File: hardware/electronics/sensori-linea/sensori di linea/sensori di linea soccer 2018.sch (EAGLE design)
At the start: 21 parts, among them T1 BP103, T2 BP103, T3 BP103, T4 BP103

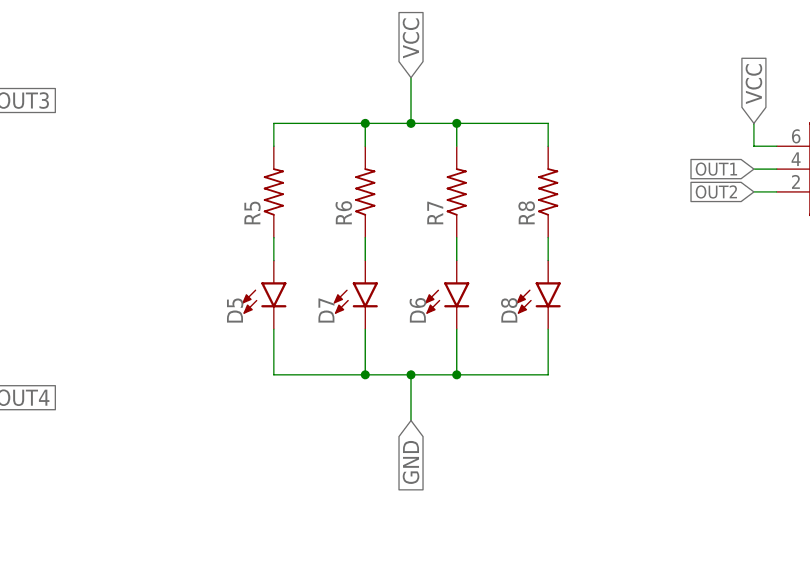
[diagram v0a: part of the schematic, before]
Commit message: modifiche a sensori di linea 2018
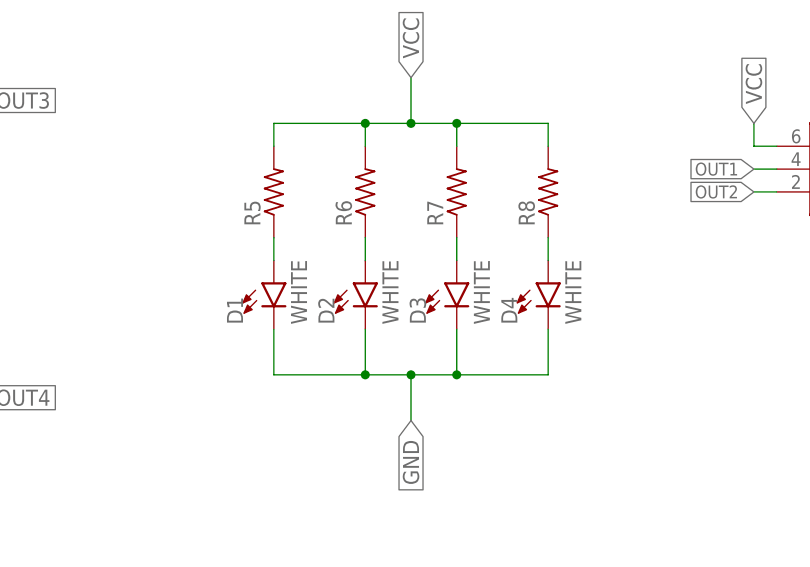
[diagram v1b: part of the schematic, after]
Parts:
- removed D5, D6, D7, D8: (no value), SparkFun-LED:LED1206
- added D1, D2, D3, D4: WHITE, SparkFun-LED:LED-WHITE1206
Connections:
- net GND: now also D1.C, D2.C, D3.C, D4.C; no longer D5.C, D6.C, D7.C, D8.C
- net N$2: now also D1.A; no longer D5.A
- net N$3: now also D2.A; no longer D7.A
- net N$4: now also D3.A; no longer D6.A
- net N$5: now also D4.A; no longer D8.A
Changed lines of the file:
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@@
 <part name="R8" library="rcl" library_urn="urn:adsk.eagle:library:334" deviceset="R-US_" device="0204/7" package3d_urn="urn:adsk.eagle:package:23498/1"/>
 <part name="SV1" library="con-lstb" library_urn="urn:adsk.eagle:library:162" deviceset="MA03-2" device="" package3d_urn="urn:adsk.eagle:package:8334/1"/>
-<part name="D5" library="SparkFun-LED" deviceset="LED" device="1206"/>
-<part name="D6" library="SparkFun-LED" deviceset="LED" device="1206"/>
-<part name="D7" library="SparkFun-LED" deviceset="LED" device="1206"/>
-<part name="D8" library="SparkFun-LED" deviceset="LED" device="1206"/>
 <part name="C1" library="SparkFun-Capacitors" deviceset="3.3NF" device="-0603-100V-10%" value="3.3nF"/>
 <part name="C2" library="SparkFun-Capacitors" deviceset="3.3NF" device="-0603-100V-10%" value="3.3nF"/>
 <part name="C3" library="SparkFun-Capacitors" deviceset="3.3NF" device="-0603-100V-10%" value="3.3nF"/>
 <part name="C4" library="SparkFun-Capacitors" deviceset="3.3NF" device="-0603-100V-10%" value="3.3nF"/>
+<part name="D1" library="SparkFun-LED" deviceset="LED-WHITE" device="1206" value="WHITE"/>
+<part name="D2" library="SparkFun-LED" deviceset="LED-WHITE" device="1206" value="WHITE"/>
+<part name="D3" library="SparkFun-LED" deviceset="LED-WHITE" device="1206" value="WHITE"/>
+<part name="D4" library="SparkFun-LED" deviceset="LED-WHITE" device="1206" value="WHITE"/>
 </parts>
 <sheets>
@@
 <instance part="R8" gate="G$1" x="185.42" y="63.5" rot="R90"/>
 <instance part="SV1" gate="1" x="218.44" y="66.04"/>
-<instance part="D5" gate="G$1" x="154.94" y="53.34"/>
-<instance part="D6" gate="G$1" x="175.26" y="53.34"/>
-<instance part="D7" gate="G$1" x="165.1" y="53.34"/>
-<instance part="D8" gate="G$1" x="185.42" y="53.34"/>
 <instance part="C1" gate="G$1" x="63.5" y="63.5"/>
 <instance part="C2" gate="G$1" x="116.84" y="63.5"/>
 <instance part="C3" gate="G$1" x="116.84" y="30.48"/>
 <instance part="C4" gate="G$1" x="63.5" y="30.48"/>
+<instance part="D1" gate="G$1" x="154.94" y="53.34"/>
+<instance part="D2" gate="G$1" x="165.1" y="53.34"/>
+<instance part="D3" gate="G$1" x="175.26" y="53.34"/>
+<instance part="D4" gate="G$1" x="185.42" y="53.34"/>
 </instances>
 <busses>
@@
 <junction x="170.18" y="43.18"/>
 <label x="170.18" y="38.1" size="1.778" layer="95" rot="R270" xref="yes"/>
-<pinref part="D5" gate="G$1" pin="C"/>
-<pinref part="D7" gate="G$1" pin="C"/>
-<pinref part="D6" gate="G$1" pin="C"/>
-<pinref part="D8" gate="G$1" pin="C"/>
+<pinref part="D1" gate="G$1" pin="C"/>
+<pinref part="D2" gate="G$1" pin="C"/>
+<pinref part="D3" gate="G$1" pin="C"/>
+<pinref part="D4" gate="G$1" pin="C"/>
 </segment>
 <segment>
@@
 <pinref part="R5" gate="G$1" pin="1"/>
 <wire x1="154.94" y1="58.42" x2="154.94" y2="55.88" width="0.1524" layer="91"/>
-<pinref part="D5" gate="G$1" pin="A"/>
+<pinref part="D1" gate="G$1" pin="A"/>
 </segment>
 </net>
@@
 <pinref part="R6" gate="G$1" pin="1"/>
 <wire x1="165.1" y1="58.42" x2="165.1" y2="55.88" width="0.1524" layer="91"/>
-<pinref part="D7" gate="G$1" pin="A"/>
+<pinref part="D2" gate="G$1" pin="A"/>
 </segment>
 </net>
@@
 <pinref part="R7" gate="G$1" pin="1"/>
 <wire x1="175.26" y1="58.42" x2="175.26" y2="55.88" width="0.1524" layer="91"/>
-<pinref part="D6" gate="G$1" pin="A"/>
+<pinref part="D3" gate="G$1" pin="A"/>
 </segment>
 </net>
@@
 <pinref part="R8" gate="G$1" pin="1"/>
 <wire x1="185.42" y1="58.42" x2="185.42" y2="55.88" width="0.1524" layer="91"/>
-<pinref part="D8" gate="G$1" pin="A"/>
-</segment>
-</net>
+<pinref part="D4" gate="G$1" pin="A"/>
+</segment>
+</net>

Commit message: modfiche
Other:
- note added: "connettore di raggruppo uscite"
- note added: "fototransistor"
- note added: "led"
- moved on the sheet: C1, C2, C3, C4, D1, D2, D3, D4, R1, R2, R3, R4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
